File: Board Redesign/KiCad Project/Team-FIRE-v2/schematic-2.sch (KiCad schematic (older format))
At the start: 20 parts, among them J4 Conn_01x03, J5 Conn_ARM_JTAG_SWD_10, U4 TXB0108DQSR, U7 TXB0104RUT

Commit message: annotated stuffff
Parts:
- gave numbers to parts that had none: 1
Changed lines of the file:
@@
 $EndComp
 $Comp
-L Team-FIRE:UX60-MB-5ST J?
+L Team-FIRE:UX60-MB-5ST J3
 U 1 1 5EAB0576
 P 4050 2650
-F 0 "J?" H 4575 2915 50  0000 C CNN
+F 0 "J3" H 4575 2915 50  0000 C CNN
 F 1 "UX60-MB-5ST" H 4575 2824 50  0000 C CNN
 F 2 "Team-FIRE:HIROSE-UX60-MB-5ST" H 5300 2700 50  0001 L CNN

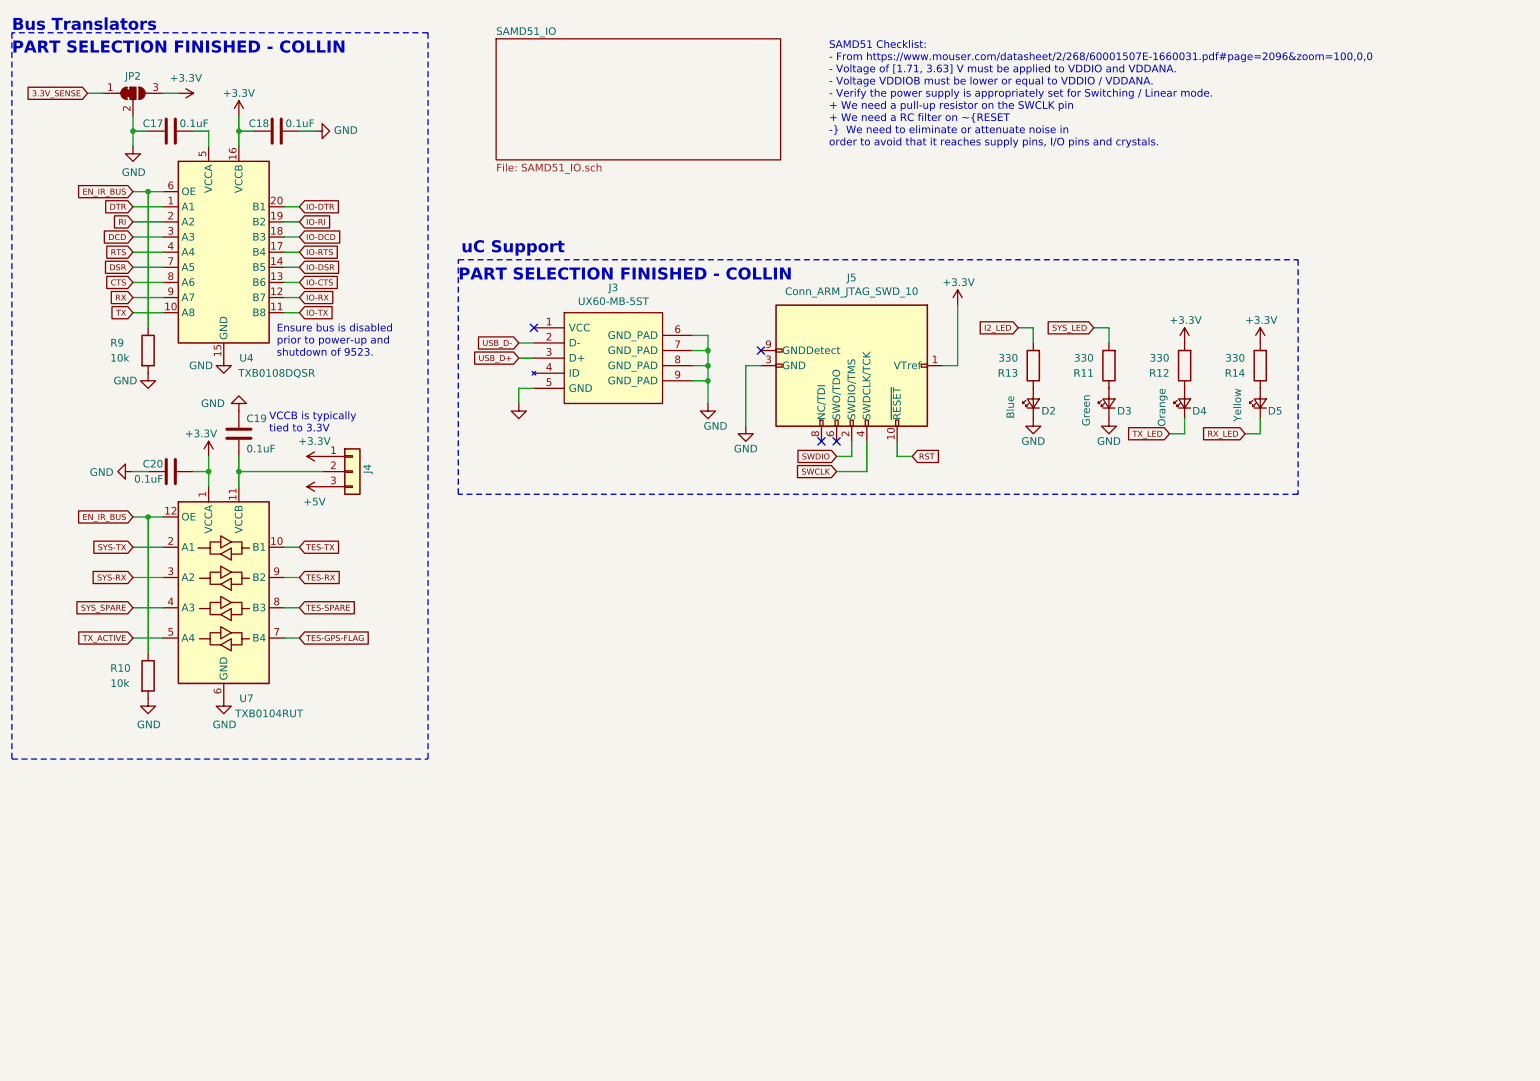
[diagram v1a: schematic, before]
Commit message: Finished SAMD part selection, fixed alignment on all sheets
- Fixed part selection for all SAMD51 sheet components
- Fixed grid misalignment in SAMD51 components
- Had to remove all SAMD51 additional text for this fix
- Added no connects to unused pins for SAMD51
- Removed component selection comments for all pages
- Add components selected except one or two boost circuit components and the SIM card connector.
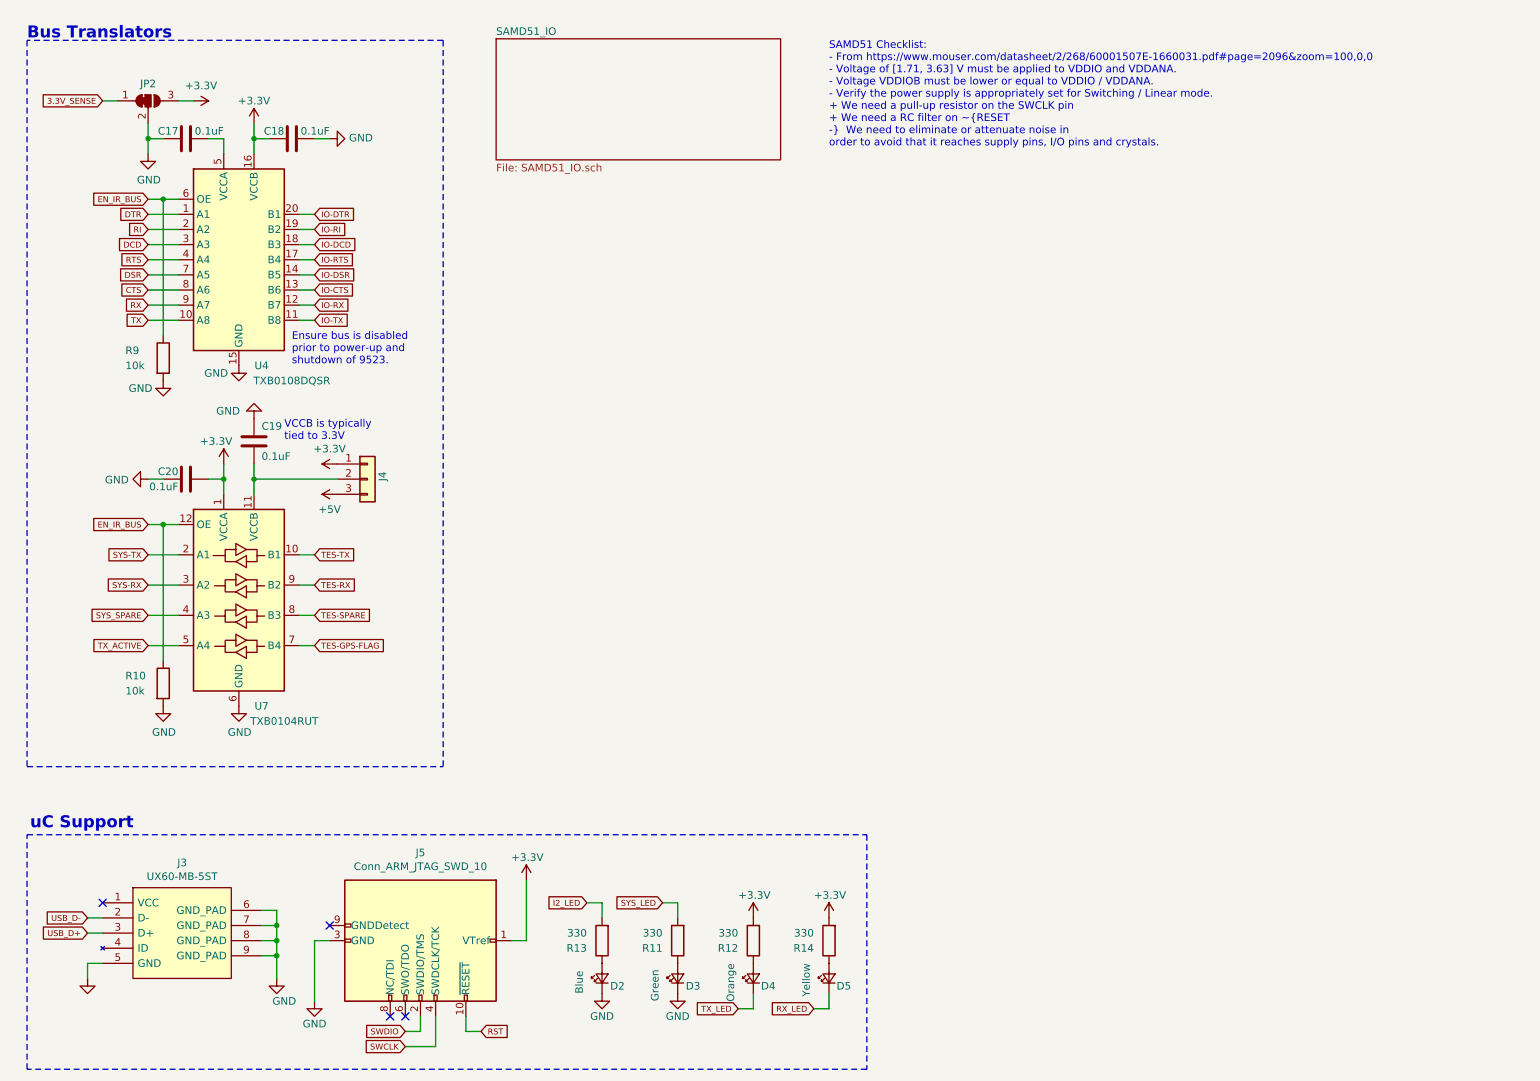
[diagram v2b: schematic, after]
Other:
- note removed: "PART SELECTION FINISHED - COLLIN"
- moved on the sheet: C17, C18, C19, C20, D2, D3, D4, D5, J3, J4, J5, JP2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
